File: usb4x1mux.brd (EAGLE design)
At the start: 145 x 80 mm, 43 parts, among them IC10 SN74LVC1G139DCTR, IC3 LDO5-3.3-SOT23, U1 LPC812M101JDH16

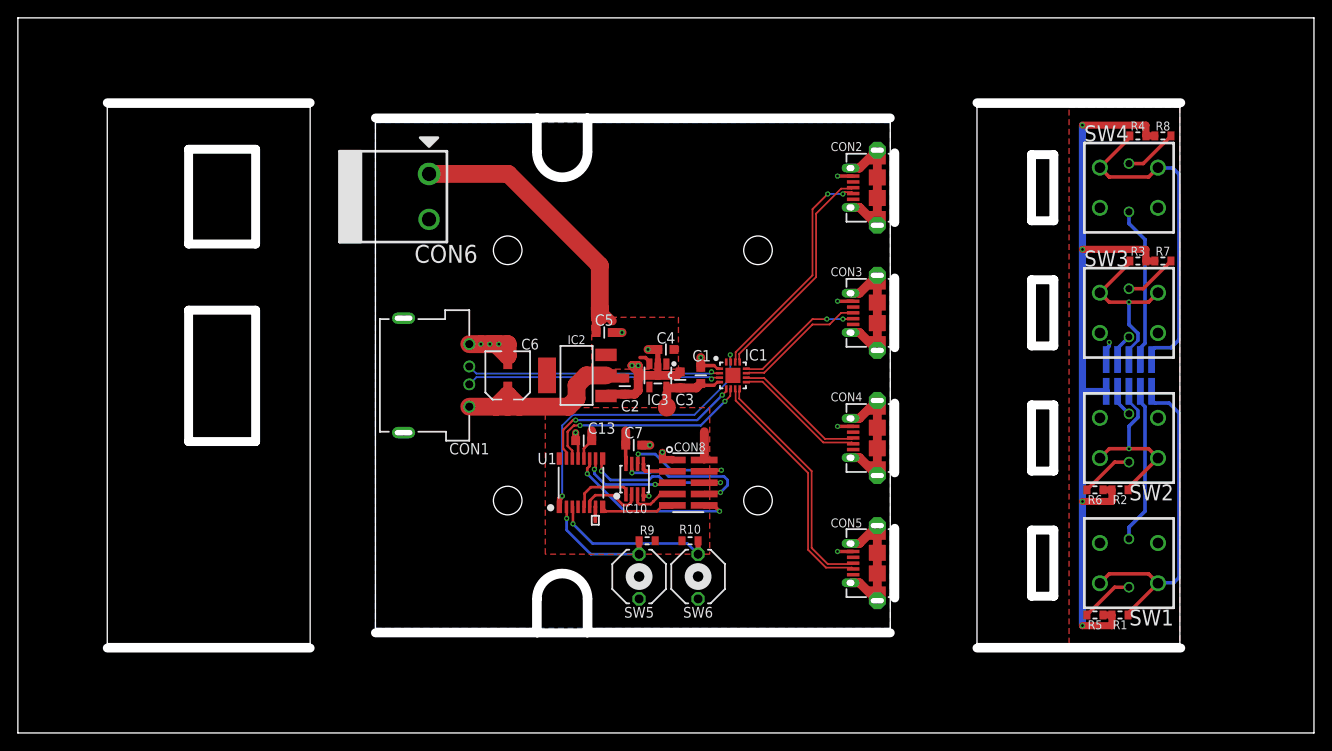
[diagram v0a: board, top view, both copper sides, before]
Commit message: update panel width
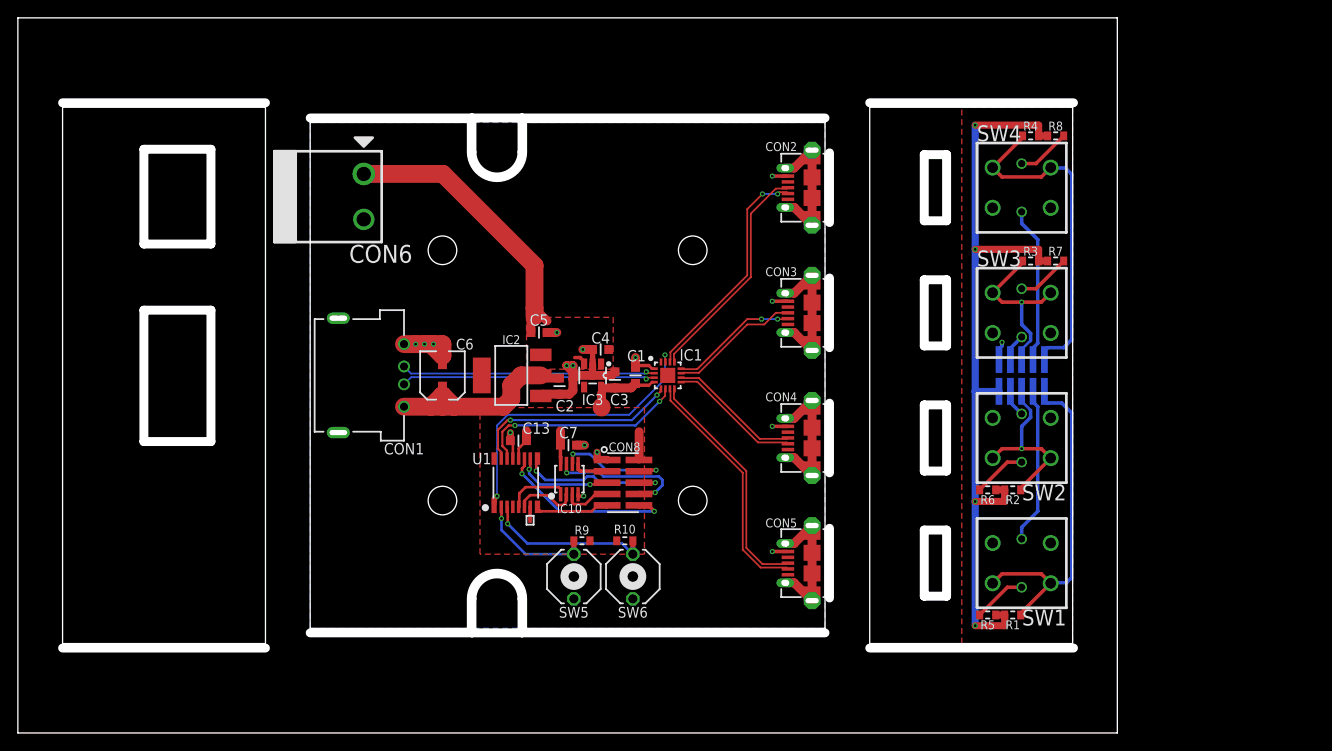
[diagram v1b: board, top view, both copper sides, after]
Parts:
- moved CON7 12.0 mm to (112.3, 40.0)
- moved PCB2 12.0 mm to (95.3, 70.0)
- moved R1 12.0 mm to (111.3, 13.2)
- moved R2 12.0 mm to (111.3, 27.2)
- moved R3 12.0 mm to (113.3, 52.8)
- moved R4 12.0 mm to (113.3, 66.8)
- moved R5 12.0 mm to (108.5, 13.2)
- moved R6 12.0 mm to (108.5, 27.2)
- moved R7 12.0 mm to (116.1, 52.8)
- moved R8 12.0 mm to (116.1, 66.8)
- moved SW1 12.0 mm to (112.3, 19.0)
- moved SW2 12.0 mm to (112.3, 33.0)
- moved SW3 12.0 mm to (112.3, 47.0)
- moved SW4 12.0 mm to (112.3, 61.0)
- moved C1 7.30 mm to (69.1, 40.0)
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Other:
- board size 145 x 80 mm -> 123 x 80 mm

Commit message: update schematic
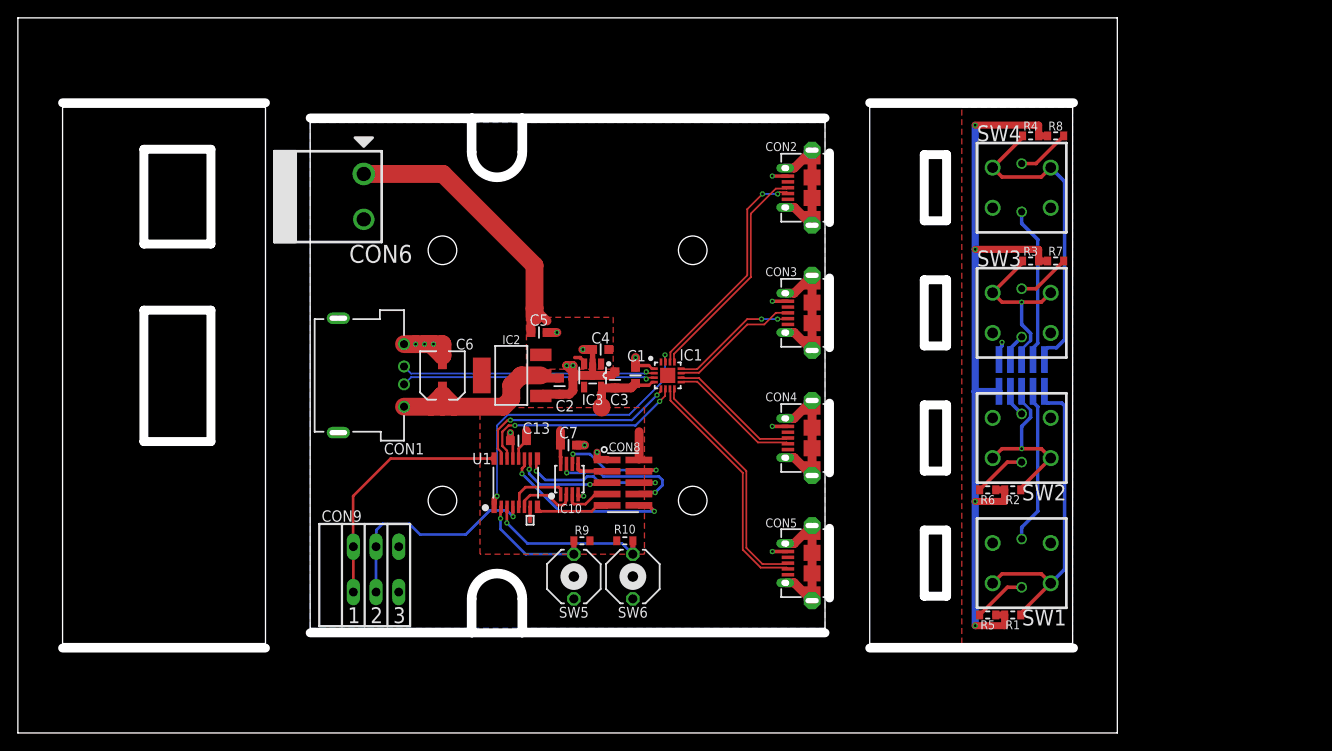
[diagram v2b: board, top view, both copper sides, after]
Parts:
- added CON9: (no value), mylib:CON-FFKV3
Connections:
- net GND: now also CON9.5, CON9.6
- net TGT_RX: now also CON9.1, CON9.2
- net TGT_TX: now also CON9.3, CON9.4
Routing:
- net TGT_RX: track 0.00 -> 29.1 mm
- net TGT_TX: track 0.00 -> 25.6 mm, vias 0 -> 1
- net SW4: track 38.1 -> 36.0 mm
- net SW1: track 40.3 -> 38.6 mm
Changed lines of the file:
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@@
 <attribute name="VALUE" x="61.5" y="32.2" size="1.27" layer="27" font="vector" ratio="15" align="center"/>
 </element>
+<element name="CON9" library="mylib" package="CON-FFKV3" value="" x="38.8" y="18.3"/>
 </elements>
 <signals>
@@
 <wire x1="65.922" y1="30.578" x2="65.9" y2="30.6" width="0.8" layer="1"/>
 <wire x1="65.9" y1="30.6" x2="64.8" y2="30.6" width="0.8" layer="1"/>
+<contactref element="CON9" pad="6"/>
+<contactref element="CON9" pad="5"/>
 </signal>
 <signal name="N$1">
@@
 <wire x1="112.2" y1="13.4" x2="115.55" y2="16.75" width="0.4" layer="1"/>
 <contactref element="CON7" pad="10"/>
-<wire x1="117.9" y1="35.8" x2="117.9" y2="17.4" width="0.4" layer="16"/>
-<wire x1="117.9" y1="17.4" x2="117.3" y2="16.8" width="0.4" layer="16"/>
-<wire x1="115.55" y1="16.75" x2="115.6" y2="16.8" width="0.4" layer="16"/>
-<wire x1="115.6" y1="16.8" x2="117.3" y2="16.8" width="0.4" layer="16"/>
 <wire x1="114.84" y1="38.222" x2="114.865" y2="39.365" width="0.4" layer="16"/>
 <wire x1="114.865" y1="39.365" x2="114.9" y2="39.4" width="0.4" layer="16"/>
@@
 <wire x1="114.9" y1="37.2" x2="115.2" y2="36.9" width="0.4" layer="16"/>
 <wire x1="115.2" y1="36.9" x2="116.8" y2="36.9" width="0.4" layer="16"/>
-<wire x1="116.8" y1="36.9" x2="117.9" y2="35.8" width="0.4" layer="16"/>
+<wire x1="116.8" y1="36.9" x2="117.1" y2="36.6" width="0.4" layer="16"/>
+<wire x1="117.1" y1="36.6" x2="117.1" y2="18.3" width="0.4" layer="16"/>
+<wire x1="117.1" y1="18.3" x2="115.55" y2="16.75" width="0.4" layer="16"/>
 </signal>
 <signal name="SW2">
@@
 <wire x1="110.1" y1="62.2" x2="109.05" y2="63.25" width="0.4" layer="1"/>
 <contactref element="CON7" pad="9"/>
-<wire x1="115.2" y1="43.1" x2="117" y2="43.1" width="0.4" layer="16"/>
-<wire x1="117" y1="43.1" x2="117.9" y2="44" width="0.4" layer="16"/>
-<wire x1="117.9" y1="44" x2="117.9" y2="62.5" width="0.4" layer="16"/>
-<wire x1="117.9" y1="62.5" x2="117.2" y2="63.2" width="0.4" layer="16"/>
-<wire x1="115.55" y1="63.25" x2="115.6" y2="63.2" width="0.4" layer="16"/>
-<wire x1="115.6" y1="63.2" x2="117.2" y2="63.2" width="0.4" layer="16"/>
+<wire x1="115.2" y1="43.1" x2="116.2" y2="43.1" width="0.4" layer="16"/>
 <wire x1="114.84" y1="41.778" x2="114.822" y2="41.778" width="0.4" layer="16"/>
 <wire x1="114.822" y1="41.778" x2="114.8" y2="41.8" width="0.4" layer="16"/>
 <wire x1="114.8" y1="41.8" x2="114.8" y2="42.7" width="0.4" layer="16"/>
 <wire x1="114.8" y1="42.7" x2="115.2" y2="43.1" width="0.4" layer="16"/>
+<wire x1="115.55" y1="63.25" x2="117.1" y2="61.7" width="0.4" layer="16"/>
+<wire x1="117.1" y1="61.7" x2="117.1" y2="44" width="0.4" layer="16"/>
+<wire x1="117.1" y1="44" x2="116.2" y2="43.1" width="0.4" layer="16"/>
 </signal>
 <signal name="N$23">
@@
 <signal name="TGT_RX">
 <contactref element="U1" pad="16"/>
+<contactref element="CON9" pad="1"/>
+<contactref element="CON9" pad="2"/>
+<wire x1="53.275" y1="30.7" x2="52.9" y2="30.7" width="0.3" layer="1"/>
+<wire x1="52.9" y1="30.7" x2="41.7" y2="30.7" width="0.3" layer="1"/>
+<wire x1="41.7" y1="30.7" x2="37.5" y2="26.5" width="0.3" layer="1"/>
+<wire x1="37.53" y1="15.76" x2="37.53" y2="20.84" width="0.3" layer="1"/>
+<wire x1="37.53" y1="20.84" x2="37.53" y2="20.87" width="0.3" layer="1"/>
+<wire x1="37.53" y1="20.87" x2="37.5" y2="20.9" width="0.3" layer="1"/>
+<wire x1="37.5" y1="20.9" x2="37.5" y2="26.5" width="0.3" layer="1"/>
+<wire x1="52.9" y1="30.7" x2="53.2" y2="31" width="0.3" layer="1"/>
+<wire x1="52.9" y1="30.7" x2="53.2" y2="30.4" width="0.3" layer="1"/>
 </signal>
 <signal name="ISP">
@@
 <contactref element="R9" pad="2"/>
 <wire x1="62.2" y1="21.5" x2="62.2" y2="20" width="0.6" layer="1"/>
-<wire x1="54.075" y1="25.3" x2="54.1" y2="25.3" width="0.3" layer="1"/>
-<wire x1="54.1" y1="25.3" x2="54.1" y2="24" width="0.3" layer="1"/>
-<wire x1="54.1" y1="24" x2="54.1" y2="22.7" width="0.3" layer="16"/>
-<wire x1="54.1" y1="22.7" x2="56.8" y2="20" width="0.3" layer="16"/>
+<wire x1="54.075" y1="25.3" x2="54" y2="25.3" width="0.3" layer="1"/>
+<wire x1="54" y1="25.3" x2="54" y2="24" width="0.3" layer="1"/>
+<wire x1="54" y1="24" x2="54" y2="22.8" width="0.3" layer="16"/>
+<wire x1="54" y1="22.8" x2="56.8" y2="20" width="0.3" layer="16"/>
 <wire x1="56.8" y1="20" x2="62.2" y2="20" width="0.3" layer="16"/>
-<via x="54.1" y="24" extent="1-16" drill="0.3"/>
+<via x="54" y="24" extent="1-16" drill="0.3"/>
 </signal>
 <signal name="!RESET!">
@@
 <contactref element="R10" pad="2"/>
 <wire x1="68.8" y1="21.5" x2="68.8" y2="20" width="0.6" layer="1"/>
-<wire x1="54.725" y1="25.3" x2="54.8" y2="25.3" width="0.3" layer="1"/>
-<wire x1="54.8" y1="25.3" x2="54.8" y2="23.4" width="0.3" layer="1"/>
-<via x="54.8" y="23.4" extent="1-16" drill="0.3"/>
-<wire x1="54.8" y1="23.4" x2="57" y2="21.2" width="0.3" layer="16"/>
+<wire x1="54.725" y1="25.3" x2="54.7" y2="25.3" width="0.3" layer="1"/>
+<wire x1="54.7" y1="25.3" x2="54.7" y2="23.5" width="0.3" layer="1"/>
+<via x="54.7" y="23.5" extent="1-16" drill="0.3"/>
+<wire x1="54.7" y1="23.5" x2="57" y2="21.2" width="0.3" layer="16"/>
 <wire x1="57" y1="21.2" x2="67.6" y2="21.2" width="0.3" layer="16"/>
 <wire x1="67.6" y1="21.2" x2="68.8" y2="20" width="0.3" layer="16"/>
@@
 <signal name="TGT_TX">
 <contactref element="U1" pad="4"/>
+<contactref element="CON9" pad="3"/>
+<contactref element="CON9" pad="4"/>
+<wire x1="55.375" y1="25.3" x2="55.4" y2="25.3" width="0.3" layer="1"/>
+<wire x1="55.4" y1="25.3" x2="55.4" y2="24.2" width="0.3" layer="1"/>
+<via x="55.4" y="24.2" extent="1-16" drill="0.3"/>
+<wire x1="55.4" y1="24.2" x2="54.7" y2="24.9" width="0.3" layer="16"/>
+<wire x1="54.7" y1="24.9" x2="52.8" y2="24.9" width="0.3" layer="16"/>
+<wire x1="52.8" y1="24.9" x2="50.1" y2="22.2" width="0.3" layer="16"/>
+<wire x1="50.1" y1="22.2" x2="45" y2="22.2" width="0.3" layer="16"/>
+<wire x1="45" y1="22.2" x2="43.8" y2="23.4" width="0.3" layer="16"/>
+<wire x1="43.8" y1="23.4" x2="40.8" y2="23.4" width="0.3" layer="16"/>
+<wire x1="40.8" y1="23.4" x2="40.1" y2="22.7" width="0.3" layer="16"/>
+<wire x1="40.07" y1="15.76" x2="40.07" y2="20.84" width="0.3" layer="16"/>
+<wire x1="40.07" y1="20.84" x2="40.07" y2="20.87" width="0.3" layer="16"/>
+<wire x1="40.07" y1="20.87" x2="40.1" y2="20.9" width="0.3" layer="16"/>
+<wire x1="40.1" y1="20.9" x2="40.1" y2="22.7" width="0.3" layer="16"/>
 </signal>
 <signal name="LSEL1">
